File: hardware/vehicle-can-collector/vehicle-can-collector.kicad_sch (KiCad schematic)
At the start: 121 parts, among them J1 OBDII Connector, Q1 DMG2301L, Q10 MMBT3904, Q11 2N7002, Q12 2N7002, Q13 2N7002, Q14 DMG2301L, Q15 2N7002, Q16 2N7002, Q2 MMBT3906, Q3 MMBT3904, Q4 DMG2301L, Q5 DMG2301L, Q6 2N7002, Q7 DMG2301L, Q8 2N7002, Q9 2N7002, U1 ATSAMC21J18A-AUT, U2 MCP2557FD-xMF, U3 LM339, U4 LMZ12001TZX-ADJ_NOPB, U5 TH8056KDC-AAA-008-RE, U6 LM317L_SOT-89, U7 LP38693MP-3.3, U8 MCP2557FD-xMF

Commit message: Added pin assignments, more datasheets
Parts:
- removed D1, D2: BAT46, Diode_THT:D_DO-35_SOD27_P7.62mm_Horizontal, symbol Diode:BAT46
- added C21: 100nF 25V, symbol Device:C
- added C? (x2): C, symbol Device:C
- added D1: BZX884B9V1L, Diode_SMD:D_0402_1005Metric_Pad0.77x0.64mm_HandSolder, symbol Device:D_Zener
- added D2: BZX884B20L, Diode_SMD:D_0402_1005Metric_Pad0.77x0.64mm_HandSolder, symbol Device:D_Zener
- added J?: I2C_STANDARD, Connector_JST:JST_PH_S4B-PH-K_1x04_P2.00mm_Horizontal, symbol SparkFun-Connectors:I2C_STANDARD
- added Q17, Q18, Q19: 2N7002, Package_TO_SOT_SMD:SOT-23, symbol Transistor_FET:2N7002
- added R57: 18k2 1%, symbol Device:R
- added R58: 10k 1%, symbol Device:R
- added R59, R60: 10k, symbol Device:R
- added RN1: 10k, Resistor_THT:R_Array_SIP9, symbol Device:R_Network08
- added U10: TCA9534, Package_SO:TSSOP-16_4.4x5mm_P0.65mm, symbol Interface_Expansion:TCA9534
- added U11: MCP2515-xSO, Package_SO:SOIC-18W_7.5x11.6mm_P1.27mm, symbol Interface_CAN_LIN:MCP2515-xSO
- added U9: AS2333Q, Package_SO:SOIC-8_3.9x4.9mm_P1.27mm, symbol Device:Opamp_Dual
- C2: value 47uF 25 Ta -> 47uF 25V Ta
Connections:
- net ANALOG_IN is gone; now on net BAT_LEVEL: C1.1, R1.2, R2.1
- net +3V3: now also U1.21 (VDDIO), U1.34 (VDDIO), U1.48 (VDDIO), U1.56 (VDDIN), U1.8 (VDDANA), C?.2, J?.2, R60.1, RN1.1 (common), U10.16 (VDD), U11.18 (VDD), U9.8 (V+)
- net GND: now also U1.22 (GND), U1.33 (GND), U1.47 (GND), U1.54 (GND), U1.7 (GNDANA), C21.2, C?.1, C?.2, D1.2 (A), D2.2 (A), J?.1, Q19.2 (S), R58.2, R59.2, U10.1 (A0), U10.2 (A1), U10.3 (A2), U10.8 (GND), U11.9 (VSS), U9.3 (+), U9.4 (V-), U9.5 (+)
- net J1850_BUS+: now also R57.1
- net J1850_TX+: now also U1.59 (PB30)
- net J1850_TX-: now also U1.60 (PB31)
- net PWM_RX: now also Q18.3 (D)
- net SW_CAN_LOAD: now also U1.38 (PA19)
- net SW_CAN_MODE0: now also U1.49 (PB22)
- net SW_CAN_MODE1: now also U1.50 (PB23)
- net SW_CAN_RX: now also U11.2 (RXCAN)
- net SW_CAN_TX: now also U11.1 (TXCAN)
- net VPW_RX: now also Q17.3 (D)
- net ~{ISO_K_RX}: now also U1.15 (PA06)
- net ~{ISO_K_TX}: now also U1.13 (PA04)
- net ~{ISO_L_TX}: now also U1.35 (PA16)
- net at U1.55 (VDDCORE): now also C?.1
- net BAT_LEVEL: now reaches U1.16 (PA07)
- net BAT_LEVEL: now also D2.1 (K), U9.1, U9.2 (-)
- net ~{OUTPUT_TX}: now reaches U1.17 (PA08)
- net ~{OUTPUT_RX}: now reaches U1.18 (PA09)
- net ~{OUTPUT_RTS}: now reaches U1.19 (PA10)
- net ~{OUTPUT_CTS}: now reaches U1.20 (PA11)
- net SW_CAN_MOSI: now reaches U1.29 (PA12)
- net SW_CAN_MOSI: now also U11.14 (SI)
- net SW_CAN_SCK: now reaches U1.30 (PA13-)
- net SW_CAN_SCK: now also U11.13 (SCK)
- net SW_CAN_CS: now reaches U1.31 (PA14)
- net SW_CAN_CS: now also U11.16 (~{CS})
- net SW_CAN_MISO: now reaches U1.32 (PA15)
- net SW_CAN_MISO: now also U11.15 (SO)
- net SW_CAN_CLK: now reaches U1.36 (PA17)
- net SW_CAN_CLK: now also U11.8 (OSC1)
- net SDA: now reaches U1.39 (PB16)
- net SDA: now also J?.3, U10.15 (SDA)
- net SCL: now reaches U1.40 (PB17)
- net SCL: now also J?.4, U10.14 (SCL)
- net ~{LINBUS_TX}: now reaches U1.41 (PA20)
- net ~{LINBUS_RX}: now reaches U1.43 (PA22)
- net SAE_PWM: now reaches U1.45 (PA24)
- net SAE_PWM: now also Q12.1 (G), R42.2, Q18.1 (G), Q19.1 (G)
- net ~{SW_CAN_INT}: now reaches U1.46 (PA25)
- net ~{SW_CAN_INT}: now also U10.13 (~{INT})
- net ~{RESET}: now reaches U1.52 (RESETN)
- net J1850_RX: now reaches U1.53 (PA28)
- net J1850_RX: now also Q17.2 (S), Q18.2 (S), R59.1
- net SWCLK: now reaches U1.57 (PA30)
- net SWDIO: now reaches U1.58 (PA31)
- net SAE_LEVEL: now reaches U1.61 (PB00)
- net SAE_LEVEL: now also C21.1, D1.1 (K), R57.2, R58.1, U9.6 (-), U9.7
- removed net PWM_~{VPW}: Q12.1 (G), Q16.1 (G), R42.2
- new net SAE_VPW: Q16.1 (G), Q17.1 (G), Q19.3 (D), R60.2
- new net SW_CAN_SOF: RN1.9 (R8), U10.12 (P7), U11.3 (CLKOUT/SOF)
- new net ~{SW_CAN_RESET}: RN1.8 (R7), U10.11 (P6), U11.17 (~{RESET})
- new net ~{SW_CAN_RX0BF}: RN1.3 (R2), U10.5 (P1), U11.11 (~{RX0BF})
- new net ~{SW_CAN_RX1BF}: RN1.4 (R3), U10.6 (P2), U11.10 (~{RX1BF})
- new net ~{SW_CAN_STATUS_INT}: RN1.2 (R1), U10.4 (P0), U11.12 (~{INT})
- new net ~{SW_CAN_TX0RTS}: RN1.5 (R4), U10.7 (P3), U11.4 (~{TX0RTS})
- new net ~{SW_CAN_TX1RTS}: RN1.6 (R5), U10.9 (P4), U11.5 (~{TX1RTS})
- new net ~{SW_CAN_TX2RTS}: RN1.7 (R6), U10.10 (P5), U11.6 (~{TX2RTS})
- no-connect marks 6 -> 31
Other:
- note added: "1.667V @ 12V 2.5V @ 18V 2.777V max @ 20V (zener)"
- note added: "1.773V @ 5V 2.482V @ 7V 3.262V max @ 9.1V (zener)"
- note added: "FUCK. XIN = PA14, XOUT = PA15, XIN32 = PA00, XOUT32 = PA01"
- note added: "I2C Address 0x20"
- note added: "J1850 Rx Multiplexor"
- note added: "SERCOM0 USART - K-Line on PA04-07 SERCOM1 USART - L-Line on PA16-19 SERCOM2 USART - OUTPUT on PA08-11 SERCOM3 USART - LINBus on PA20-23 SERCOM4 SPI - SW-CAN on PA12-15 SERCOM5 I2C - SW-CAN on PB16-17 GCLKIO3 - SW-CAN clock gen on PA17 TCC0 - SAE J1850 I/O on PB30-31 EXTINT8 - SAE J1850 Rx on PA28 EXTINT13 - SW-CAN IRQ on PA25 AIN0 - SAE_LEVEL on PB00 (ADC1) AIN7 - BAT_LEVEL on PA07 (ADC0) SWCLK/S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"
- note added: "Single-Wire CAN Controller"
- moved on the sheet: C1, C14, Q11, R1, R2, R27, R28, R29, R33, R36, R51, U1A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

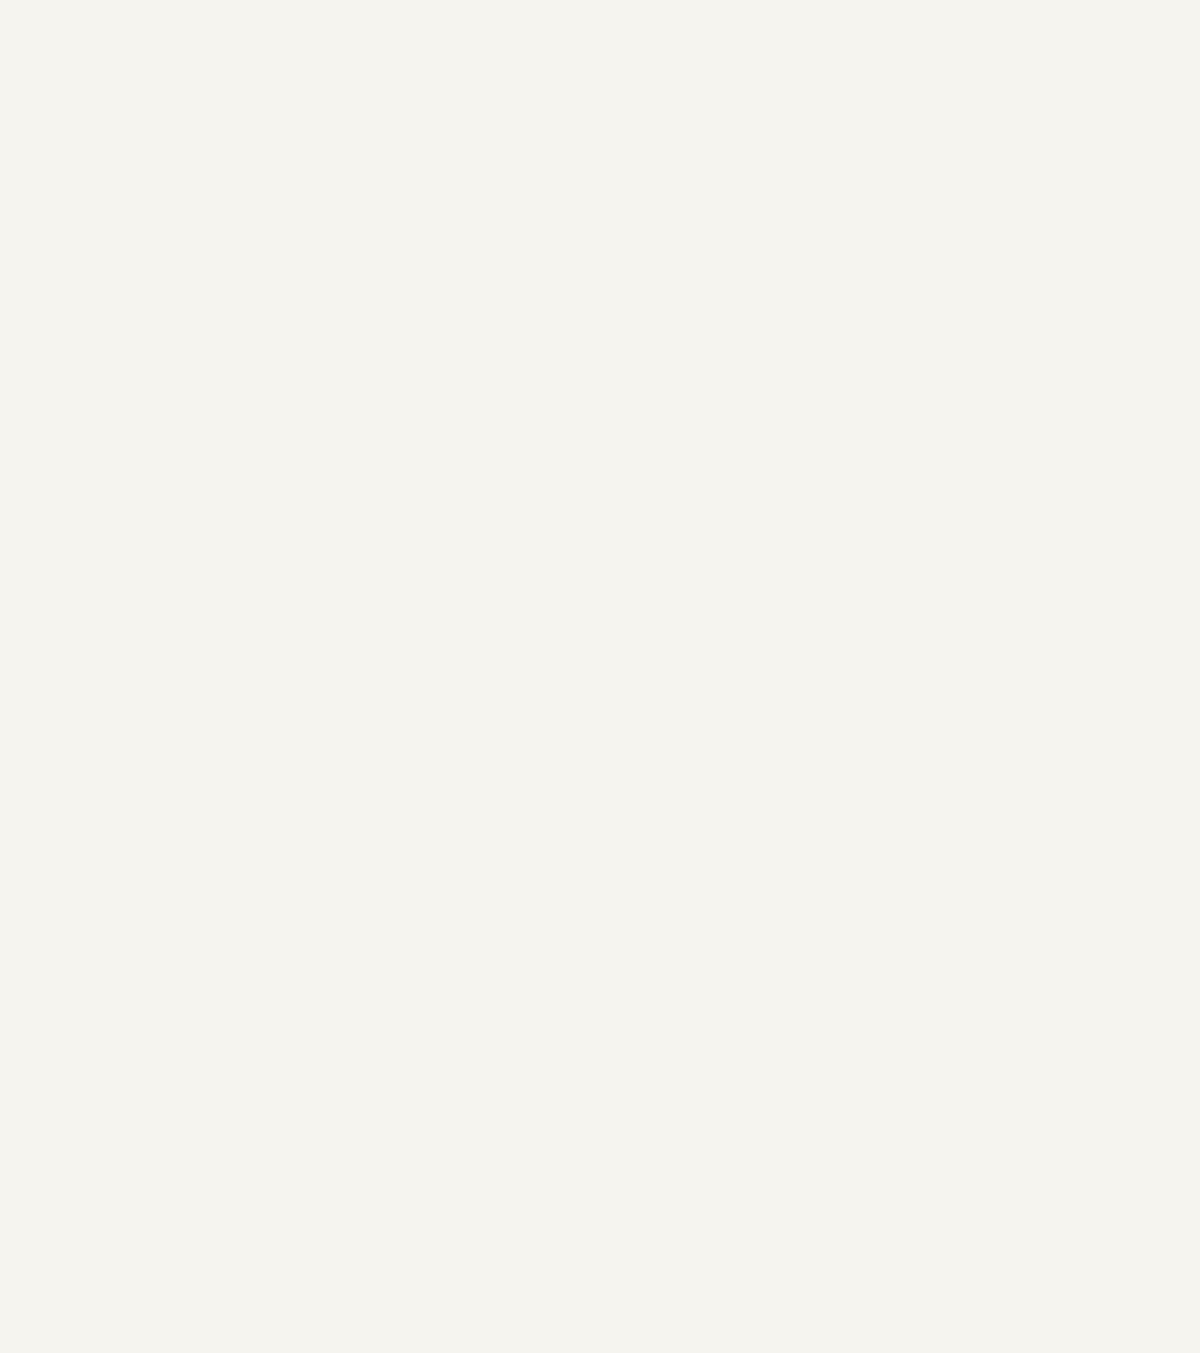
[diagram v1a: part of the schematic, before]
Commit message: Add FT2232H for debug + serial output on USB
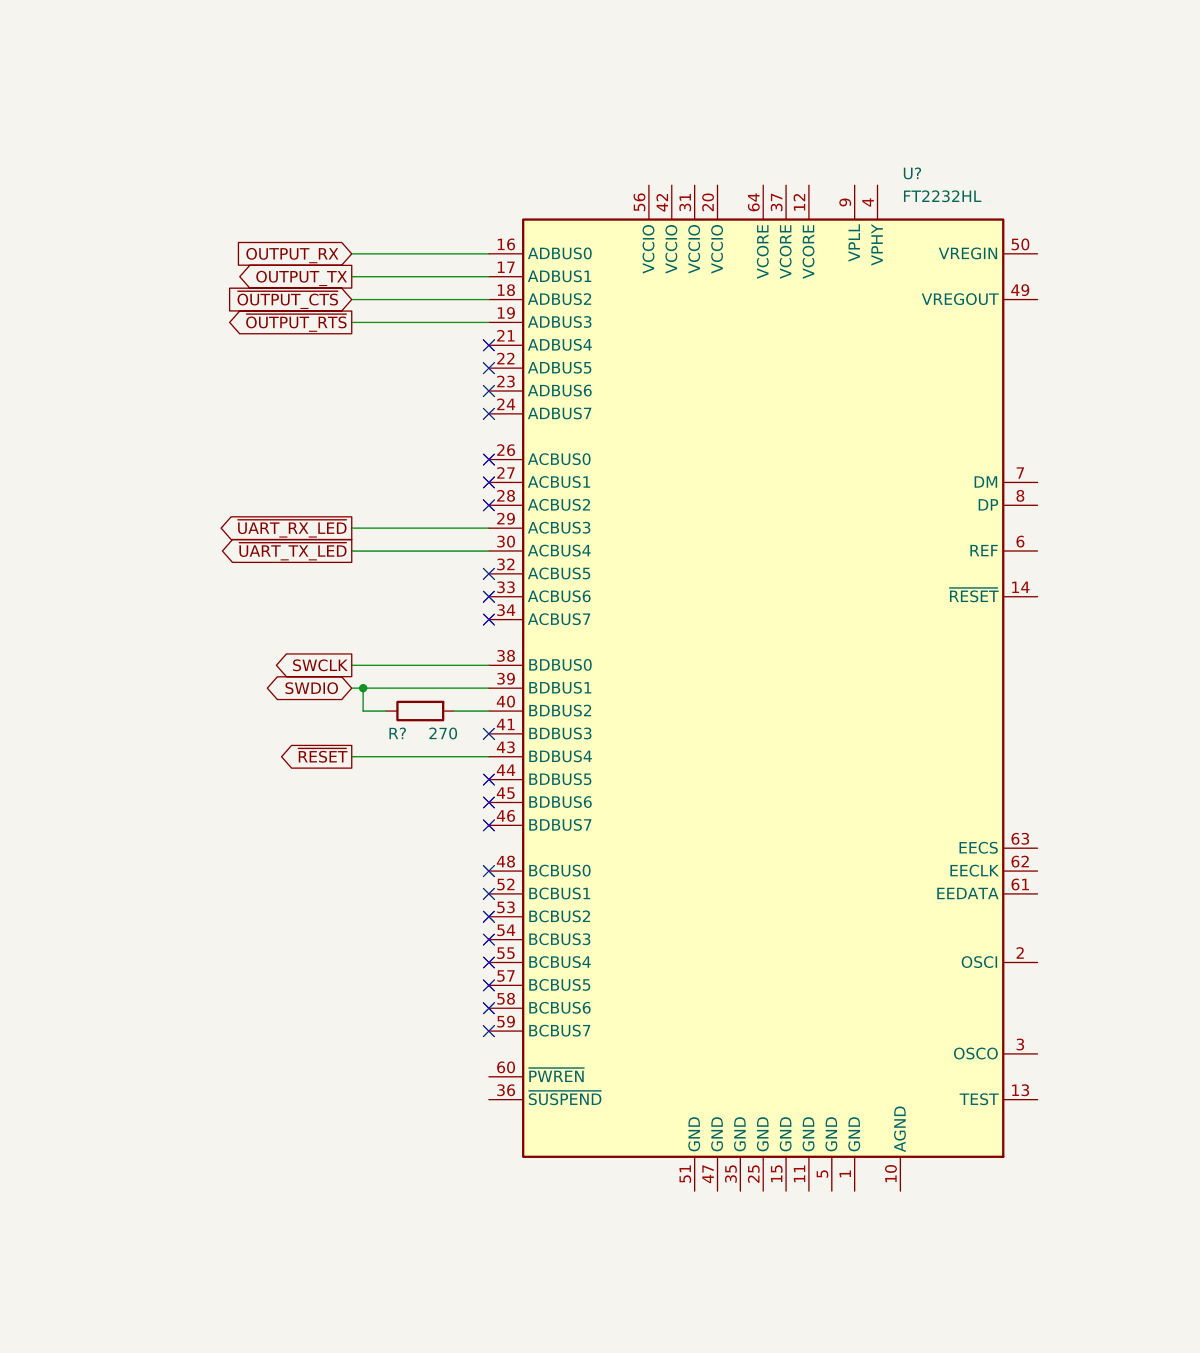
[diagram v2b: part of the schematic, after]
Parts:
- added R?: 270, symbol Device:R
- added U?: FT2232HL, Package_QFP:LQFP-64_10x10mm_P0.5mm, symbol Interface_USB:FT2232HL
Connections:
- net SWCLK: now also U?.38 (BDBUS0)
- net SWDIO: now also R?.1, U?.39 (BDBUS1)
- net ~{OUTPUT_CTS}: now also U?.18 (ADBUS2)
- net ~{OUTPUT_RTS}: now also U?.19 (ADBUS3)
- net ~{RESET}: now also U?.43 (BDBUS4)
- new net: R?.2, U?.40 (BDBUS2)
- new net OUTPUT_RX: U?.16 (ADBUS0)
- new net OUTPUT_TX: U?.17 (ADBUS1)
- new net ~{UART_RX_LED}: U?.29 (ACBUS3)
- new net ~{UART_TX_LED}: U?.30 (ACBUS4)
- no-connect marks 31 -> 53

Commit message: Reannotate
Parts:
- gave numbers to parts that had none: 5
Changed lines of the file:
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@@
   (symbol (lib_id "Device:R") (at 373.38 125.73 90) (mirror x) (unit 1)
     (in_bom yes) (on_board yes)
-    (property "Reference" "R?" (id 0) (at 370.84 128.27 90))
+    (property "Reference" "R61" (id 0) (at 370.84 128.27 90))
     (property "Value" "270" (id 1) (at 375.92 128.27 90))
     (property "Footprint" "" (id 2) (at 373.38 123.952 90)
@@
   (symbol (lib_id "power:+3V3") (at 195.58 38.1 0) (unit 1)
     (in_bom yes) (on_board yes) (fields_autoplaced)
-    (property "Reference" "#PWR?" (id 0) (at 195.58 41.91 0)
+    (property "Reference" "#PWR088" (id 0) (at 195.58 41.91 0)
       (effects (font (size 1.27 1.27)) hide)
     )
@@
   (symbol (lib_id "power:+3V3") (at 389.89 387.35 0) (unit 1)
     (in_bom yes) (on_board yes) (fields_autoplaced)
-    (property "Reference" "#PWR?" (id 0) (at 389.89 391.16 0)
+    (property "Reference" "#PWR090" (id 0) (at 389.89 391.16 0)
       (effects (font (size 1.27 1.27)) hide)
     )
@@
   (symbol (lib_id "Device:C") (at 184.15 52.07 0) (unit 1)
     (in_bom yes) (on_board yes) (fields_autoplaced)
-    (property "Reference" "C?" (id 0) (at 187.96 50.7999 0)
+    (property "Reference" "C22" (id 0) (at 187.96 50.7999 0)
       (effects (font (size 1.27 1.27)) (justify left))
     )
@@
   (symbol (lib_id "Interface_USB:FT2232HL") (at 411.48 123.19 0) (mirror y) (unit 1)
     (in_bom yes) (on_board yes) (fields_autoplaced)
-    (property "Reference" "U?" (id 0) (at 426.9487 66.04 0)
+    (property "Reference" "U12" (id 0) (at 426.9487 66.04 0)
       (effects (font (size 1.27 1.27)) (justify right))
     )
@@
   (symbol (lib_id "Device:C") (at 193.04 62.23 0) (mirror x) (unit 1)
     (in_bom yes) (on_board yes) (fields_autoplaced)
-    (property "Reference" "C?" (id 0) (at 189.23 60.9599 0)
+    (property "Reference" "C23" (id 0) (at 189.23 60.9599 0)
       (effects (font (size 1.27 1.27)) (justify right))
     )
@@
   (symbol (lib_id "power:GND") (at 184.15 55.88 0) (unit 1)
     (in_bom yes) (on_board yes)
-    (property "Reference" "#PWR?" (id 0) (at 184.15 62.23 0)
+    (property "Reference" "#PWR087" (id 0) (at 184.15 62.23 0)
       (effects (font (size 1.27 1.27)) hide)
     )
@@
   (symbol (lib_id "power:GND") (at 389.89 403.86 0) (unit 1)
     (in_bom yes) (on_board yes) (fields_autoplaced)
-    (property "Reference" "#PWR?" (id 0) (at 389.89 410.21 0)
+    (property "Reference" "#PWR091" (id 0) (at 389.89 410.21 0)
       (effects (font (size 1.27 1.27)) hide)
     )
@@
   (symbol (lib_id "SparkFun-Connectors:I2C_STANDARD") (at 377.19 402.59 0) (unit 1)
     (in_bom yes) (on_board yes) (fields_autoplaced)
-    (property "Reference" "J?" (id 0) (at 379.095 384.81 0))
+    (property "Reference" "J2" (id 0) (at 379.095 384.81 0))
     (property "Value" "I2C_STANDARD" (id 1) (at 379.095 387.35 0))
     (property "Footprint" "Connector_JST:JST_PH_S4B-PH-K_1x04_P2.00mm_Horizontal" (id 2) (at 377.952 398.78 0)
@@
   (symbol (lib_id "power:GND") (at 195.58 78.74 0) (unit 1)
     (in_bom yes) (on_board yes) (fields_autoplaced)
-    (property "Reference" "#PWR?" (id 0) (at 195.58 85.09 0)
+    (property "Reference" "#PWR089" (id 0) (at 195.58 85.09 0)
       (effects (font (size 1.27 1.27)) hide)
     )
@@
       (reference "#PWR086") (unit 1) (value "GND") (footprint "")
     )
+    (path "/d16175d6-e93f-435e-b1c7-bcd772d3cee7"
+      (reference "#PWR087") (unit 1) (value "GND") (footprint "")
+    )
     (path "/59e98602-d19a-4d9d-a65f-5fd996827f00"
-      (reference "#PWR?") (unit 1) (value "+3V3") (footprint "")
+      (reference "#PWR088") (unit 1) (value "+3V3") (footprint "")
+    )
+    (path "/fa9c2881-cb5e-4b76-a953-7e67a694cec1"
+      (reference "#PWR089") (unit 1) (value "GND") (footprint "")
     )
     (path "/5c78bed6-c707-4238-8a81-86476f8ae91a"
-      (reference "#PWR?") (unit 1) (value "+3V3") (footprint "")
-    )
-    (path "/d16175d6-e93f-435e-b1c7-bcd772d3cee7"
-      (reference "#PWR?") (unit 1) (value "GND") (footprint "")
+      (reference "#PWR090") (unit 1) (value "+3V3") (footprint "")
     )
     (path "/d74c6336-d7dd-494f-8095-0fc57da1646d"
-      (reference "#PWR?") (unit 1) (value "GND") (footprint "")
-    )
-    (path "/fa9c2881-cb5e-4b76-a953-7e67a694cec1"
-      (reference "#PWR?") (unit 1) (value "GND") (footprint "")
+      (reference "#PWR091") (unit 1) (value "GND") (footprint "")
     )
     (path "/00000000-0000-0000-0000-000063ae8b1c"
@@
     )
     (path "/685d7a49-95c0-4604-a46a-fb3bc5bd3878"
-      (reference "C?") (unit 1) (value "C") (footprint "")
+      (reference "C22") (unit 1) (value "C") (footprint "")
     )
     (path "/b6d5dfb0-24c7-43cd-9b20-15faadb175f6"
-      (reference "C?") (unit 1) (value "C") (footprint "")
+      (reference "C23") (unit 1) (value "C") (footprint "")
     )
     (path "/435dd551-cb9e-47a1-adf2-b16742698cd2"
@@
     )
     (path "/e0ab9c4f-618f-4e11-a69a-a621ed21a122"
-      (reference "J?") (unit 1) (value "I2C_STANDARD") (footprint "Connector_JST:JST_PH_S4B-PH-K_1x04_P2.00mm_Horizontal")
+      (reference "J2") (unit 1) (value "I2C_STANDARD") (footprint "Connector_JST:JST_PH_S4B-PH-K_1x04_P2.00mm_Horizontal")
     )
     (path "/00000000-0000-0000-0000-000063b17a01"
@@
     )
     (path "/3ef777f2-6669-4a59-9c9c-22e78adeb935"
-      (reference "R?") (unit 1) (value "270") (footprint "")
+      (reference "R61") (unit 1) (value "270") (footprint "")
     )
     (path "/aef95ed8-ced2-47f5-948f-5e223b7f48a1"
@@
     )
     (path "/802fdeea-eab5-4f34-ad4d-d37d80a9b2a3"
-      (reference "U?") (unit 1) (value "FT2232HL") (footprint "Package_QFP:LQFP-64_10x10mm_P0.5mm")
-    )
-  )
+      (reference "U12") (unit 1) (value "FT2232HL") (footprint "Package_QFP:LQFP-64_10x10mm_P0.5mm")
+    )
+  )

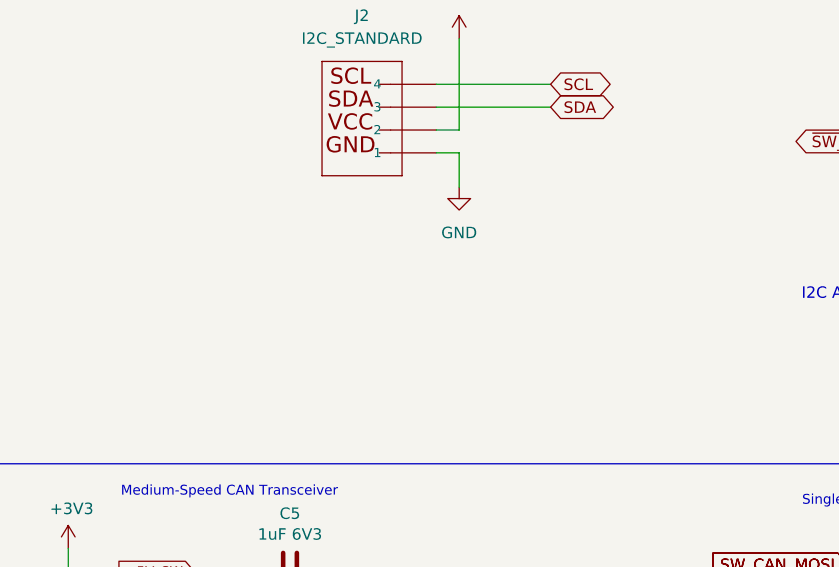
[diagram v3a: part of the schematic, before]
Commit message: Add QWIIC connector
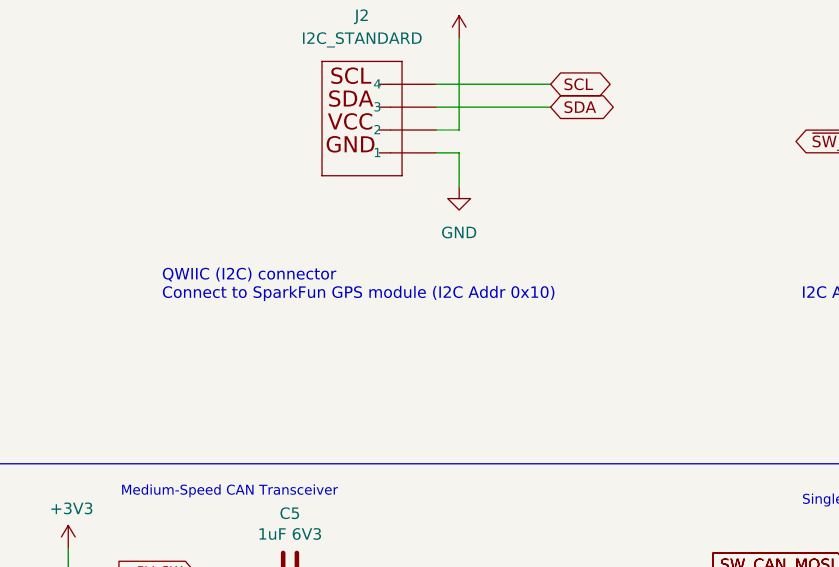
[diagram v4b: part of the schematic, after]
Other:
- note added: "QWIIC (I2C) connector Connect to SparkFun GPS module (I2C Addr 0x10)"
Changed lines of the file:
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@@
     (effects (font (size 1.0922 1.0922)) (justify right bottom))
+  )
+  (text "QWIIC (I2C) connector\nConnect to SparkFun GPS module (I2C Addr 0x10)"
+    (at 356.87 416.56 0)
+    (effects (font (size 1.27 1.27)) (justify left bottom))
   )
   (text "Single-Wire CAN Controller" (at 427.99 439.42 0)
